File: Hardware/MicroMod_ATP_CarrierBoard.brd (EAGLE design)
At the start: 86.4 x 55.9 mm, 206 parts, among them J19 QWIIC_RIGHT_ANGLE, J2 JTAG, J20 QWIIC_RIGHT_ANGLE, J21 1X04_SMD_STRAIGHT_COMBO, J4 USB_A_SMT_FEMALE, J6 MICROMOD-2222-C, J8 1X04_SMD_STRAIGHT_COMBO, U5 AP7361C-33

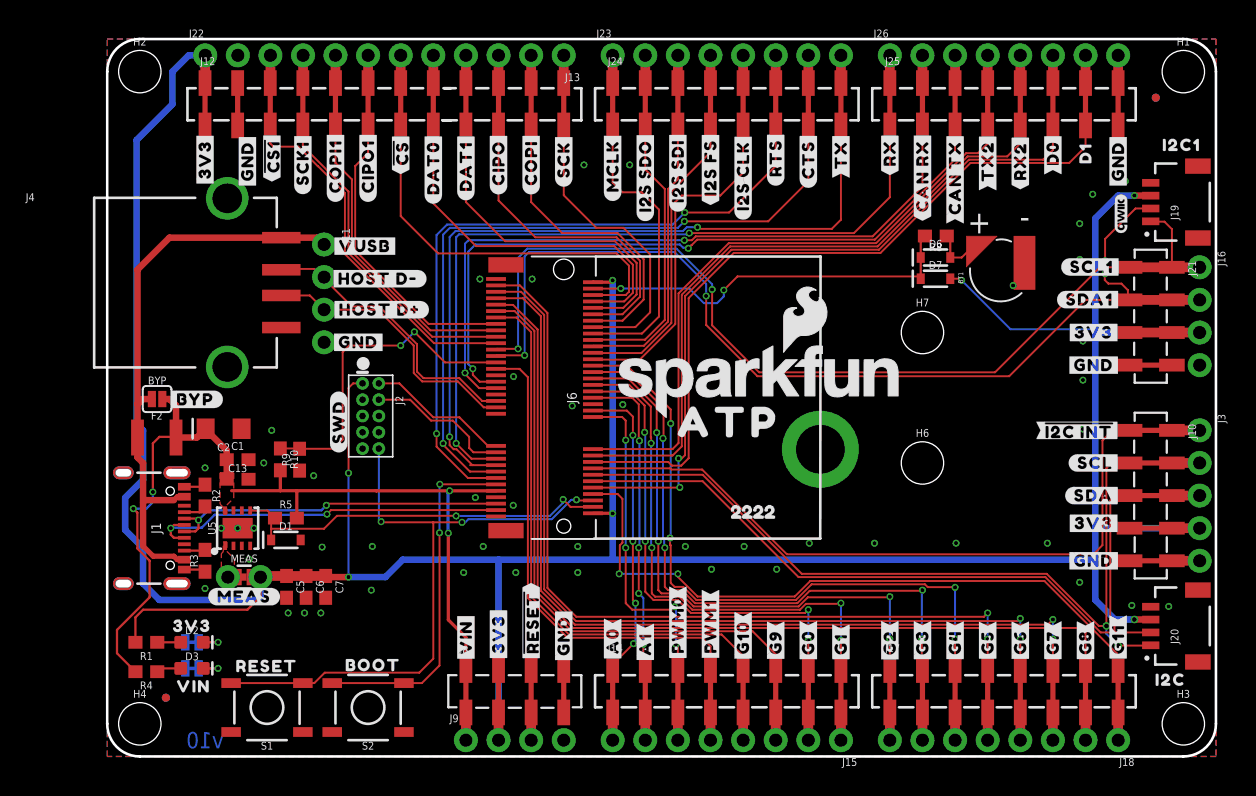
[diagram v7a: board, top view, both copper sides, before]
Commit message: Changes silk labels to bi-directional on G# lines, fixes INPUT/OUTPUT labels on
RTS, CTS, A#, and PWM lines
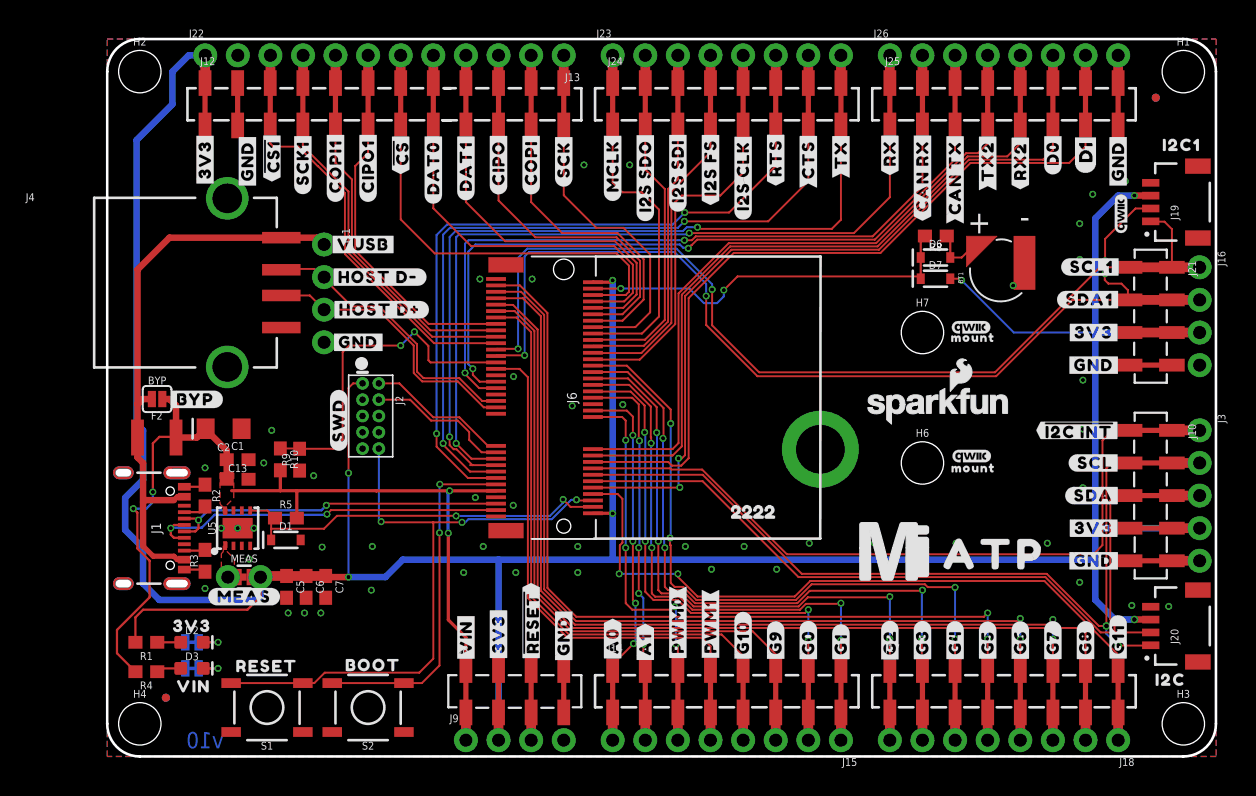
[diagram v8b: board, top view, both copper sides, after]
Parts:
- added LOGO5, LOGO6, LOGO7, LOGO8: QWIIC_LOGO_3MM, SparkFun-Aesthetics:QWIIC_3MM
- added U$140: (no value), SparkFun-MicroMod:MICROMOD_MI_LOGO_1
- added U$141, U$142, U$143: (no value), headtop:MOUNT10
- added U$144: (no value), SparkFun-MicroMod:MICROMOD_LOGO_1
- added U$99: (no value), D1:D10
- LOGO1: value SFE_LOGO_NAME_FLAME.2_INCH -> SFE_LOGO_NAME_FLAME.1_INCH; device SparkFun-Aesthetics:SFE_LOGO_NAME_FLAME_.2 -> SparkFun-Aesthetics:SFE_LOGO_NAME_FLAME_.1
- U$139: device ana:D11 -> headtop:MOUNT10
- moved U$62 23.1 mm to (69.1, 15.7)
- moved U$139 16.8 mm to (67.4, 32.6), turned to 0 degrees
- moved LOGO1 14.1 mm to (64.8, 27.3)
- moved LOGO4 1.14 mm to (35.9, 32.6)
- moved U$73 0.97 mm to (35.8, 21.7)
- moved U$70 0.38 mm to (76.8, 17.8)
- moved U$130 0.18 mm to (19.9, 39.9)
- moved U$50 0.18 mm to (19.9, 39.9)
- moved U$129 0.13 mm to (21.1, 37.3)
- moved U$131 0.13 mm to (18.0, 26.2)
- moved U$41 0.13 mm to (21.1, 37.3)
- moved U$51 0.13 mm to (18.0, 26.2)
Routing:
- net VIN/3: track 25.6 -> 26.2 mm
